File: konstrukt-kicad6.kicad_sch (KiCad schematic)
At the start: 0 parts

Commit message: PSU schem capture done
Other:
- added sheet PSU (psu.kicad_sch)
- sheet LFO ports: added +9Vd; removed none

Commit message: PSU schem update
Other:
- sheet 2xDelay ports: added +9Vd; removed none
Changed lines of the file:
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@@
+    (stroke (width 0) (type default) (color 0 0 0 0))
+  )
+  (wire (pts (xy 270.51 20.32) (xy 270.51 25.4))
     (stroke (width 0) (type default) (color 0 0 0 0))
   )
@@
   )
   (label "+9Vd" (at 25.4 161.29 180)
+    (effects (font (size 1.27 1.27)) (justify right bottom))
+  )
+  (label "+9Vd" (at 270.51 20.32 180)
     (effects (font (size 1.27 1.27)) (justify right bottom))
   )
@@
     (pin "+4.5V" input (at 257.81 35.56 180)
       (effects (font (size 1.27 1.27)) (justify left))
+    )
+    (pin "+9Vd" input (at 270.51 25.4 90)
+      (effects (font (size 1.27 1.27)) (justify right))
     )
   )
@@
       (reference "C2804") (unit 1) (value "100n") (footprint "Capacitor_SMD:CP_Elec_4x5.4")
     )
-    (path "/e28f6215-25d3-404f-a4ff-7314b3a215a8/0a4ae053-d382-4ab1-a397-64995e3d7dc5"
-      (reference "C2805") (unit 1) (value "10n") (footprint "Capacitor_SMD:CP_Elec_6.3x5.3")
+    (path "/e28f6215-25d3-404f-a4ff-7314b3a215a8/ba675edf-7a66-4301-bbe2-8249a51d9072"
+      (reference "C2805") (unit 1) (value "22u") (footprint "Capacitor_SMD:CP_Elec_6.3x5.3")
     )
     (path "/e28f6215-25d3-404f-a4ff-7314b3a215a8/cebef319-7a65-47bf-9e3a-61121d88d185"

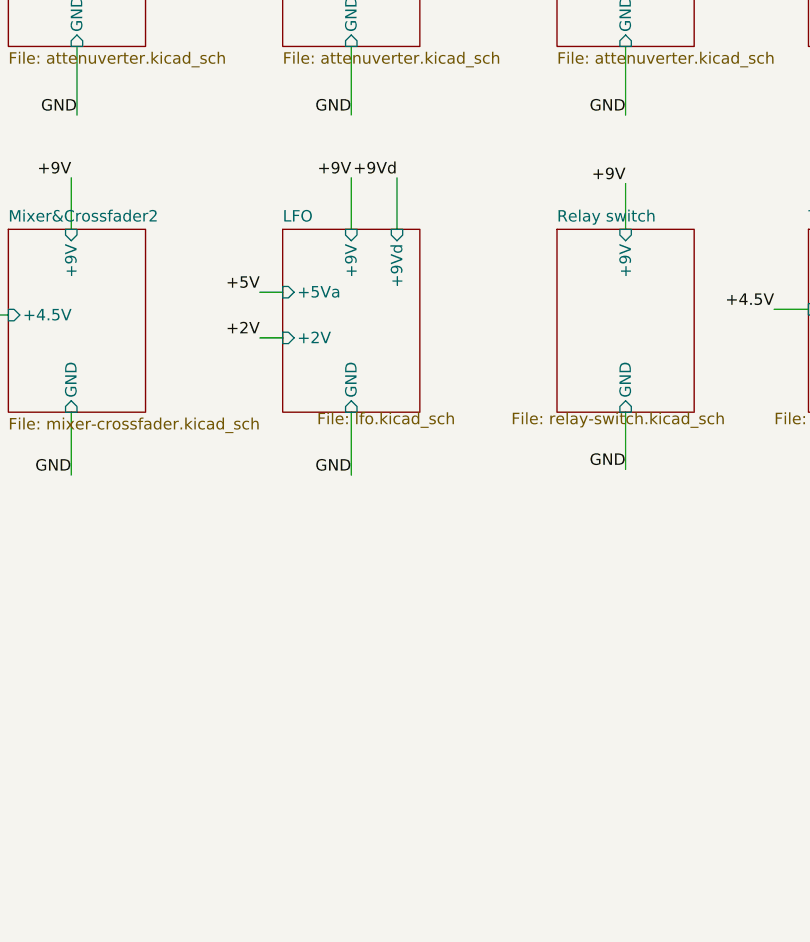
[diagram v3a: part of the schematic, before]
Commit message: Jacks schem done
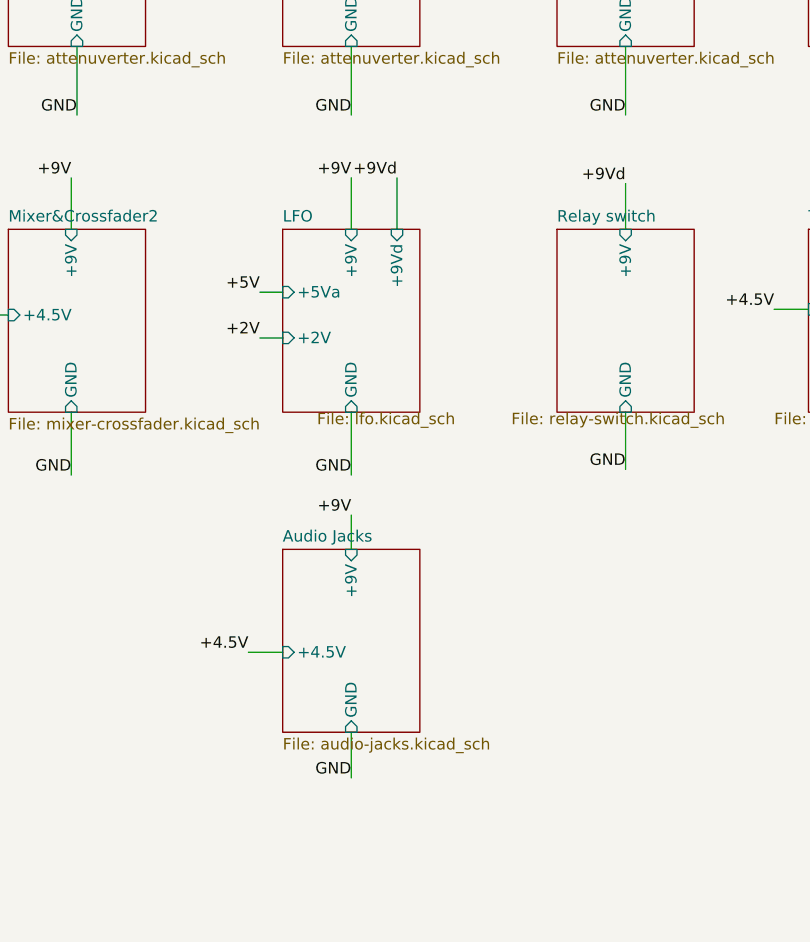
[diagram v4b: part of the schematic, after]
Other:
- added sheet Audio Jacks (audio-jacks.kicad_sch)

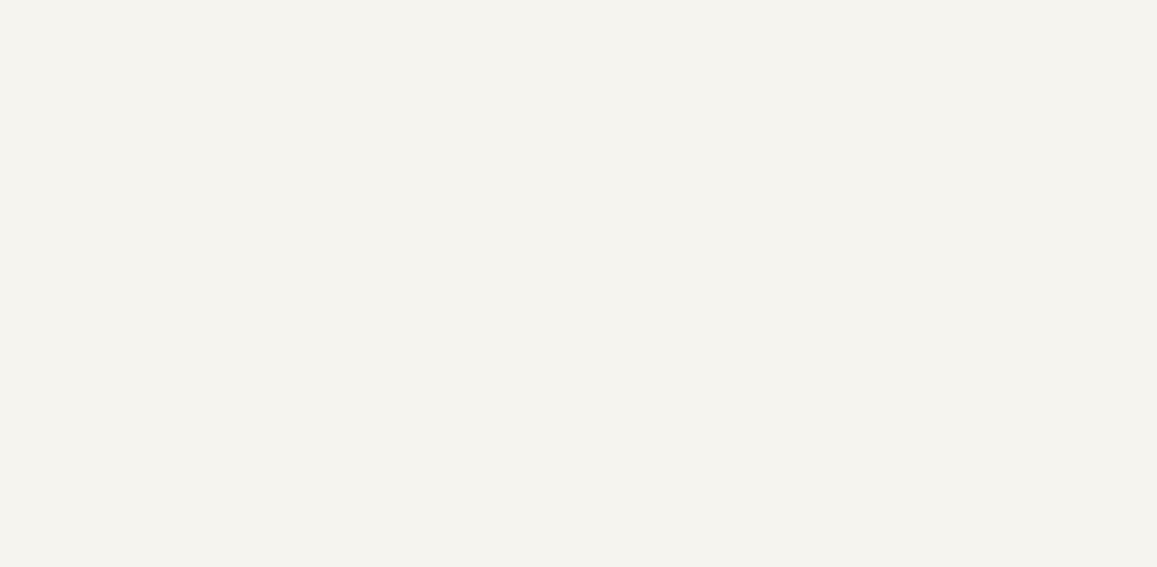
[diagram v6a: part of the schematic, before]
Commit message: Add mounting holes
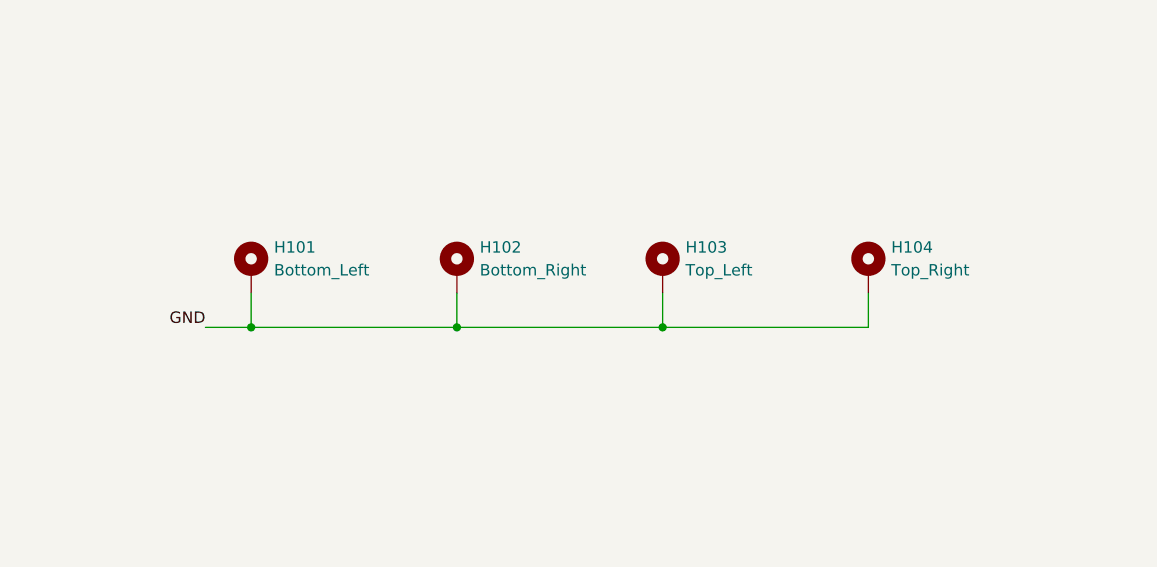
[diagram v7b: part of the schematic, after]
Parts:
- added H101: Bottom_Left, MountingHole:MountingHole_3.2mm_M3_Pad_TopBottom, symbol Mechanical:MountingHole_Pad
- added H102: Bottom_Right, MountingHole:MountingHole_3.2mm_M3_Pad_TopBottom, symbol Mechanical:MountingHole_Pad
- added H103: Top_Left, MountingHole:MountingHole_3.2mm_M3_Pad_TopBottom, symbol Mechanical:MountingHole_Pad
- added H104: Top_Right, MountingHole:MountingHole_3.2mm_M3_Pad_TopBottom, symbol Mechanical:MountingHole_Pad
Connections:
- net GND: now also H101.1, H102.1, H103.1, H104.1
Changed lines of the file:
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@@
 (kicad_sch (version 20211123) (generator eeschema)
   (paper "A4")
+  (junction (at 93.98 165.1) (diameter 0) (color 0 0 0 0)
+  )
+  (junction (at 71.12 165.1) (diameter 0) (color 0 0 0 0)
+  )
+  (junction (at 116.84 165.1) (diameter 0) (color 0 0 0 0)
+  )
   (wire (pts (xy 97.79 60.325) (xy 97.79 66.04))
     (stroke (width 0) (type default) (color 0 0 0 0))
@@
     (stroke (width 0) (type default) (color 0 0 0 0))
   )
+  (wire (pts (xy 139.7 161.29) (xy 139.7 165.1))
+    (stroke (width 0) (type default) (color 0 0 0 0))
+  )
   (wire (pts (xy 228.6 59.69) (xy 228.6 66.04))
     (stroke (width 0) (type default) (color 0 0 0 0))
@@
     (stroke (width 0) (type default) (color 0 0 0 0))
   )
+  (wire (pts (xy 93.98 165.1) (xy 71.12 165.1))
+    (stroke (width 0) (type default) (color 0 0 0 0))
+  )
   (wire (pts (xy 156.21 45.72) (xy 156.21 53.34))
     (stroke (width 0) (type default) (color 0 0 0 0))
@@
     (stroke (width 0) (type default) (color 0 0 0 0))
   )
+  (wire (pts (xy 71.12 165.1) (xy 66.04 165.1))
+    (stroke (width 0) (type default) (color 0 0 0 0))
+  )
   (wire (pts (xy 40.64 105.41) (xy 45.085 105.41))
     (stroke (width 0) (type default) (color 0 0 0 0))
@@
     (stroke (width 0) (type default) (color 0 0 0 0))
   )
+  (wire (pts (xy 93.98 161.29) (xy 93.98 165.1))
+    (stroke (width 0) (type default) (color 0 0 0 0))
+  )
+  (wire (pts (xy 139.7 165.1) (xy 116.84 165.1))
+    (stroke (width 0) (type default) (color 0 0 0 0))
+  )
   (wire (pts (xy 40.64 107.95) (xy 45.085 107.95))
     (stroke (width 0) (type default) (color 0 0 0 0))
@@
     (stroke (width 0) (type default) (color 0 0 0 0))
   )
+  (wire (pts (xy 116.84 161.29) (xy 116.84 165.1))
+    (stroke (width 0) (type default) (color 0 0 0 0))
+  )
   (wire (pts (xy 265.43 20.32) (xy 265.43 25.4))
     (stroke (width 0) (type default) (color 0 0 0 0))
@@
     (stroke (width 0) (type default) (color 0 0 0 0))
   )
+  (wire (pts (xy 71.12 161.29) (xy 71.12 165.1))
+    (stroke (width 0) (type default) (color 0 0 0 0))
+  )
   (wire (pts (xy 228.6 45.72) (xy 228.6 53.34))
     (stroke (width 0) (type default) (color 0 0 0 0))
@@
   )
   (wire (pts (xy 187.325 45.72) (xy 187.325 53.34))
+    (stroke (width 0) (type default) (color 0 0 0 0))
+  )
+  (wire (pts (xy 116.84 165.1) (xy 93.98 165.1))
     (stroke (width 0) (type default) (color 0 0 0 0))
   )
@@
   )
   (label "GND" (at 187.325 53.34 180)
+    (effects (font (size 1.27 1.27)) (justify right bottom))
+  )
+  (label "GND" (at 66.04 165.1 180)
     (effects (font (size 1.27 1.27)) (justify right bottom))
   )
@@
     (pin "1")
   )
+  (symbol (lib_id "Mechanical:MountingHole_Pad") (at 71.12 158.75 0) (unit 1)
+    (in_bom yes) (on_board yes) (fields_autoplaced)
+    (property "Reference" "H101" (id 0) (at 73.66 156.2099 0)
+      (effects (font (size 1.27 1.27)) (justify left))
+    )
+    (property "Value" "Bottom_Left" (id 1) (at 73.66 158.7499 0)
+      (effects (font (size 1.27 1.27)) (justify left))
+    )
+    (property "Footprint" "MountingHole:MountingHole_3.2mm_M3_Pad_TopBottom" (id 2) (at 71.12 158.75 0)
+      (effects (font (size 1.27 1.27)) hide)
+    )
+    (property "Datasheet" "~" (id 3) (at 71.12 158.75 0)
+      (effects (font (size 1.27 1.27)) hide)
+    )
+    (pin "1")
+  )
   (symbol (lib_id "power:PWR_FLAG") (at 38.1 177.8 0) (unit 1)
     (in_bom yes) (on_board yes) (fields_autoplaced)
@@
     (pin "1")
   )
+  (symbol (lib_id "Mechanical:MountingHole_Pad") (at 139.7 158.75 0) (unit 1)
+    (in_bom yes) (on_board yes) (fields_autoplaced)
+    (property "Reference" "H104" (id 0) (at 142.24 156.2099 0)
+      (effects (font (size 1.27 1.27)) (justify left))
+    )
+    (property "Value" "Top_Right" (id 1) (at 142.24 158.7499 0)
+      (effects (font (size 1.27 1.27)) (justify left))
+    )
+    (property "Footprint" "MountingHole:MountingHole_3.2mm_M3_Pad_TopBottom" (id 2) (at 139.7 158.75 0)
+      (effects (font (size 1.27 1.27)) hide)
+    )
+    (property "Datasheet" "~" (id 3) (at 139.7 158.75 0)
+      (effects (font (size 1.27 1.27)) hide)
+    )
+    (pin "1")
+  )
+  (symbol (lib_id "Mechanical:MountingHole_Pad") (at 116.84 158.75 0) (unit 1)
+    (in_bom yes) (on_board yes) (fields_autoplaced)
+    (property "Reference" "H103" (id 0) (at 119.38 156.2099 0)
+      (effects (font (size 1.27 1.27)) (justify left))
+    )
+    (property "Value" "Top_Left" (id 1) (at 119.38 158.7499 0)
+      (effects (font (size 1.27 1.27)) (justify left))
+    )
+    (property "Footprint" "MountingHole:MountingHole_3.2mm_M3_Pad_TopBottom" (id 2) (at 116.84 158.75 0)
+      (effects (font (size 1.27 1.27)) hide)
+    )
+    (property "Datasheet" "~" (id 3) (at 116.84 158.75 0)
+      (effects (font (size 1.27 1.27)) hide)
+    )
+    (pin "1")
+  )
   (symbol (lib_id "power:PWR_FLAG") (at 38.1 170.18 0) (unit 1)
     (in_bom yes) (on_board yes) (fields_autoplaced)
@@
     )
     (property "Datasheet" "~" (id 3) (at 38.1 184.15 0)
+      (effects (font (size 1.27 1.27)) hide)
+    )
+    (pin "1")
+  )
+  (symbol (lib_id "Mechanical:MountingHole_Pad") (at 93.98 158.75 0) (unit 1)
+    (in_bom yes) (on_board yes) (fields_autoplaced)
+    (property "Reference" "H102" (id 0) (at 96.52 156.2099 0)
+      (effects (font (size 1.27 1.27)) (justify left))
+    )
+    (property "Value" "Bottom_Right" (id 1) (at 96.52 158.7499 0)
+      (effects (font (size 1.27 1.27)) (justify left))
+    )
+    (property "Footprint" "MountingHole:MountingHole_3.2mm_M3_Pad_TopBottom" (id 2) (at 93.98 158.75 0)
+      (effects (font (size 1.27 1.27)) hide)
+    )
+    (property "Datasheet" "~" (id 3) (at 93.98 158.75 0)
       (effects (font (size 1.27 1.27)) hide)
     )
@@
       (reference "FB2801") (unit 1) (value "FerriteBead") (footprint "Resistor_SMD:R_0805_2012Metric_Pad1.20x1.40mm_HandSolder")
     )
+    (path "/3060943a-5f7e-474a-8595-cd101d7c123d"
+      (reference "H101") (unit 1) (value "Bottom_Left") (footprint "MountingHole:MountingHole_3.2mm_M3_Pad_TopBottom")
+    )
+    (path "/fe2b4e54-fc72-4a20-bf83-a42af16005a5"
+      (reference "H102") (unit 1) (value "Bottom_Right") (footprint "MountingHole:MountingHole_3.2mm_M3_Pad_TopBottom")
+    )
+    (path "/9d7318d1-6eb3-44b5-a3e0-51fe43508832"
+      (reference "H103") (unit 1) (value "Top_Left") (footprint "MountingHole:MountingHole_3.2mm_M3_Pad_TopBottom")
+    )
+    (path "/91732995-3211-4891-88b4-9f540a620925"
+      (reference "H104") (unit 1) (value "Top_Right") (footprint "MountingHole:MountingHole_3.2mm_M3_Pad_TopBottom")
+    )
     (path "/a20b1572-4a1d-447e-be8c-a6218de04c26/61bd750c-d666-47c5-a035-f0b3fb6f4f6e"
